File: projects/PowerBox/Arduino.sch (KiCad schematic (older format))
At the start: 59 parts, among them CON3 USB-MINI-B-Vert, IC2 OPAMP-DUALU, P10 CONN_4, P11 CONN_10, P12 CONN_8, P13 CONN_8, P14 CONN_6, P15 CONN_4, P7 CONN_3X2, P8 CONN_4, P9 CONN_4, Q1 MOSFET-P, U3 INA219, U4 AP7333, U5 ATMEGA32U4, X1 16MHz

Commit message: small modifications
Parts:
- added Q?: MOSFET-P, symbol MOSFET-P
- added VR? (x2): VR, symbol VR
- C?: renamed from C5; value 4u7F -> 10uF
- R?: renamed from R21; value 33R -> 22R
- R?: renamed from R22; value 33R -> 22R
- renumbered C3 to C?, C7 to C?, C6 to C?, C12 to C?, C14 to C?, C2 to C?, C1 to C?, C4 to C?, C8 to C?, C9 to C?, C10 to C?, C11 to C?, C13 to C?, CON3 to CON?, D3 to D?, D4 to D?, D5 to D?, D6 to D?, D7 to D?, F1 to F?, IC2 to IC?, JP4 to JP?, JP5 to JP?, JP3 to JP?, L1 to L?, N1 to N?, N2 to N?, N3 to N?, N4 to N?, P11 to P?, P12 to P?, P13 to P?, P14 to P?, P7 to P?, P9 to P?, P10 to P?, P15 to P?, P8 to P?, Q1 to Q?, R24 to R?, R23 to R?, R30 to R?, R28 to R?, R27 to R?, R26 to R?, R29 to R?, R31 to R?, R19 to R?, R20 to R?, R25 to R?, S4 to S?, S5 to S?, U5 to U?, U4 to U?, U3 to U?, X1 to X?
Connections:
- net 3V3: now also IC?.5 (+IN)
- net VREG_in: now also Q?.2 (S); no longer IC?.3 (+IN)
- net XTAL2: now reaches C?.1, R?.2, U?.16 (XTAL2), X?.1
- net XTAL1: now reaches C?.1, R?.1, U?.17 (XTAL1), X?.2
- net at U?.3 (D-): now also R?.2; no longer R?.1
- net at CON?.2 (D-): now also VR?.1; no longer R?.2
- net at R?.2: now also VR?.2; no longer CON?.3 (D+)
- net VCC: now reaches IC?.6 (-IN)
- net VCC: now also IC?.3 (+IN), Q?.3 (D)
- net at IC?.7 (OUT): now also Q?.1 (G)
- new net: R?.1, VR?.2
- new net: CON?.3 (D+), VR?.1
- no-connect marks 10 -> 7
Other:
- note added: "transistor is conducting, when Vgs < 0"
- moved on the sheet: C?, IC?B, JP?, P?, R?, X?

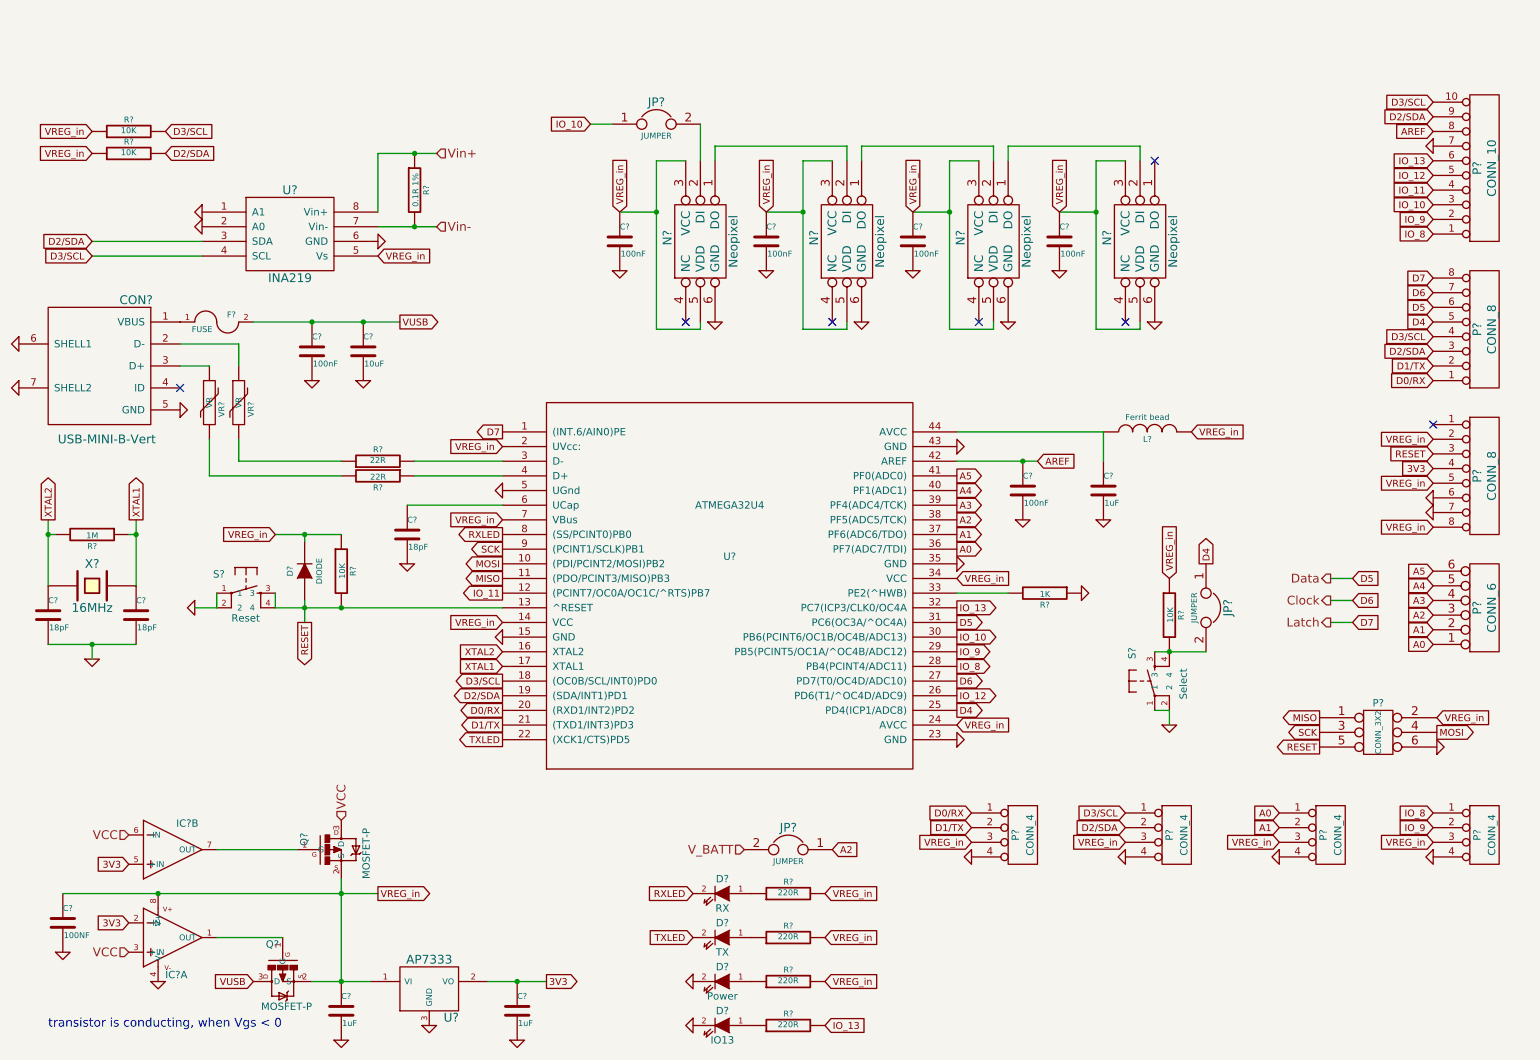
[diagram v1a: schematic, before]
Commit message: erc warnings solved
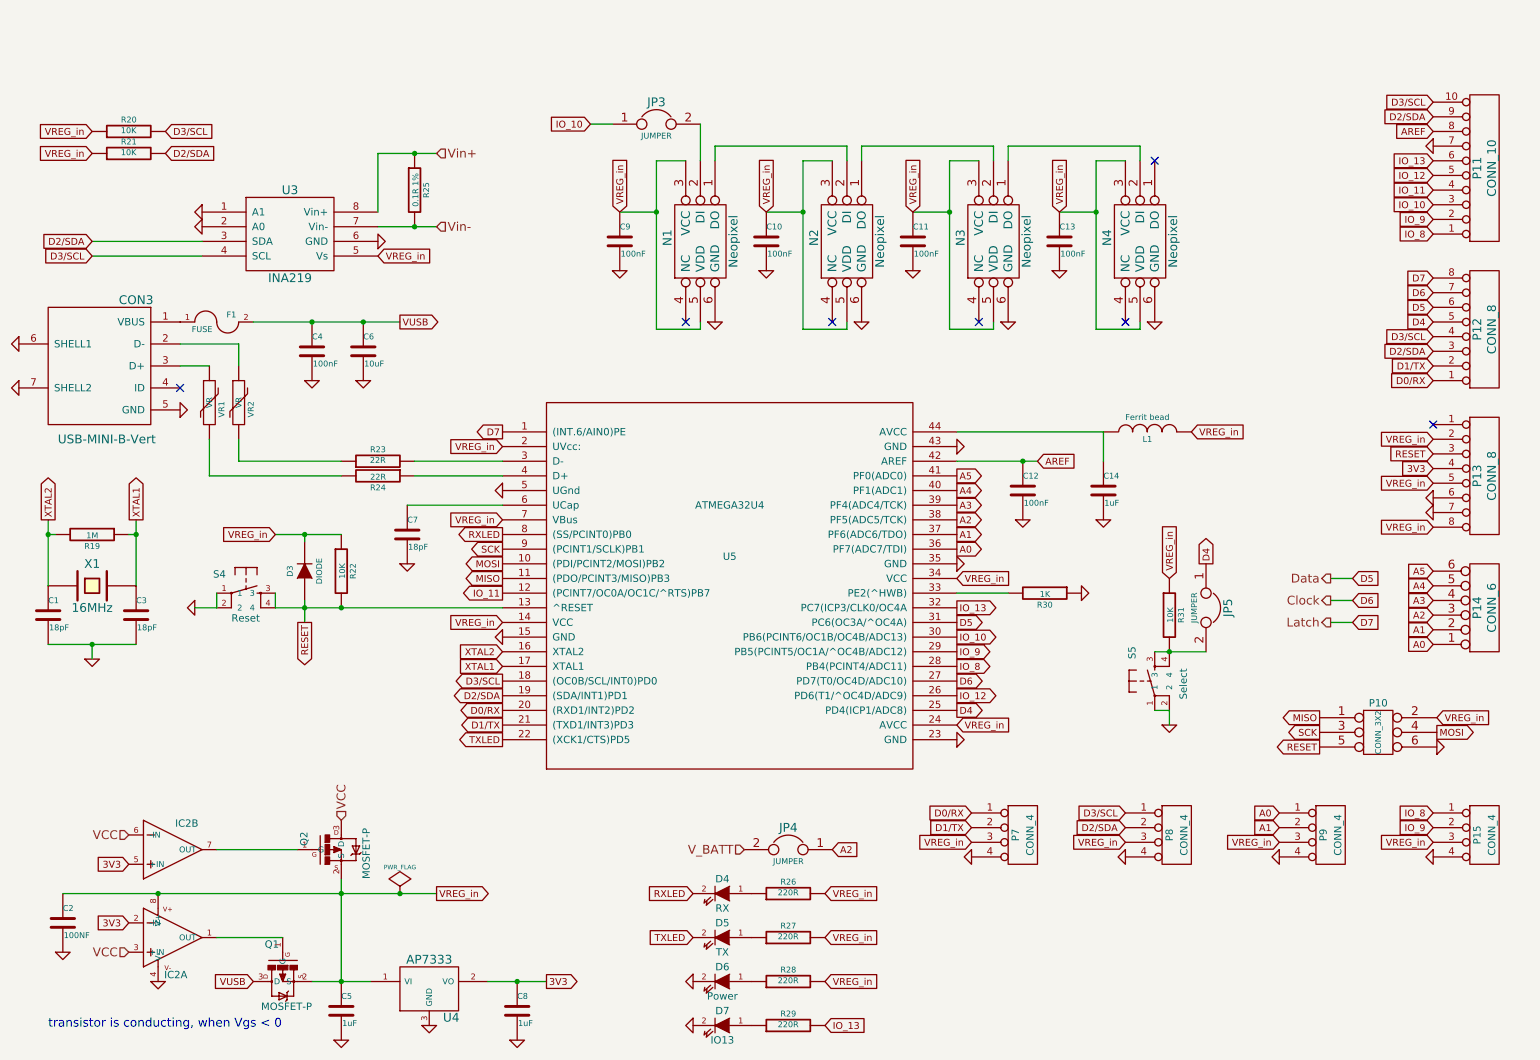
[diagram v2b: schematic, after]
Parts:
- gave numbers to parts that had none: 62

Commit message: more footprints added
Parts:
- C1, C10, C11, C12, C13, C14, C2, C3, C4, C5, C6, C7, C8, C9: footprint (none) -> frep:C0805
- CON3: footprint (none) -> frep:Vertical_USB_Mini_B
- D3, D4, D5, D6, D7: footprint (none) -> frep:LED-0805
- F1, R25: footprint (none) -> frep:R1206
- IC2: footprint SparkFun-SO08 -> frep:SOIC8
- JP3, JP4, JP5: footprint (none) -> frep:Pin_Proto_Straight_1x02
- L1, R19, R20, R21, R22, R23, R24, R26, R27, R28, R29, R30, R31, VR1, VR2: footprint (none) -> frep:R0805
- N1, N2, N3, N4: footprint (none) -> frep:Neopixel
- P10: footprint (none) -> frep:Pin_Proto_Straight_2x03
- P11: footprint (none) -> frep:Pin_Header_Straight_1x10
- P12, P13: footprint (none) -> frep:Pin_Header_Angled_1x08
- P14: footprint (none) -> frep:Pin_Header_Straight_1x06
- P15, P7, P8, P9: footprint (none) -> frep:grove_con_straight
- Q1, Q2, U4: footprint (none) -> frep:SOT23
- S4, S5: footprint TACTILE -> frep:TACTILE-PTH
- U3: footprint (none) -> frep:SOIC8
- U5: footprint MODULE -> frep:TQFP44
- X1: footprint (none) -> frep:HC49UP

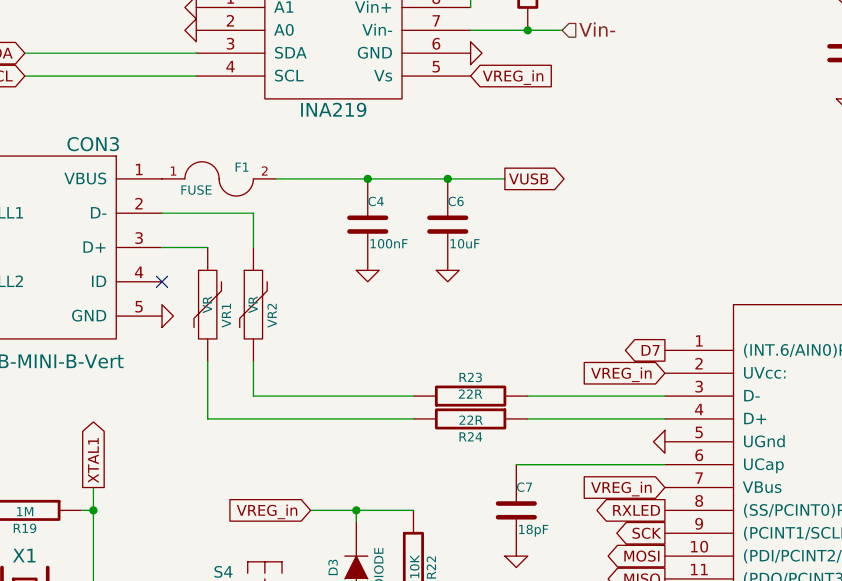
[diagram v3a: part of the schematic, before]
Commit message: protection parts added
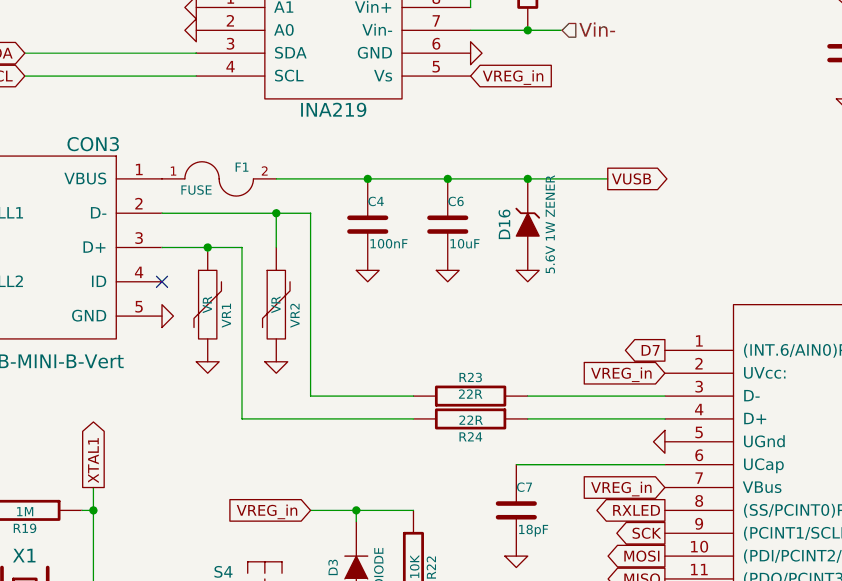
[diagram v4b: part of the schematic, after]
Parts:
- added D16: 5.6V 1W ZENER, symbol ZENER
- F1: footprint frep:R1206 -> frep:C1812
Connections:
- net GND: now also VR1.2, VR2.2, D16.1 (A)
- net VUSB: now also D16.2 (K)
- net at R23.1: now also CON3.2 (D-), VR2.1; no longer VR2.2
- net at R24.2: now also CON3.3 (D+), VR1.1; no longer VR1.2
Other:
- moved on the sheet: VR2

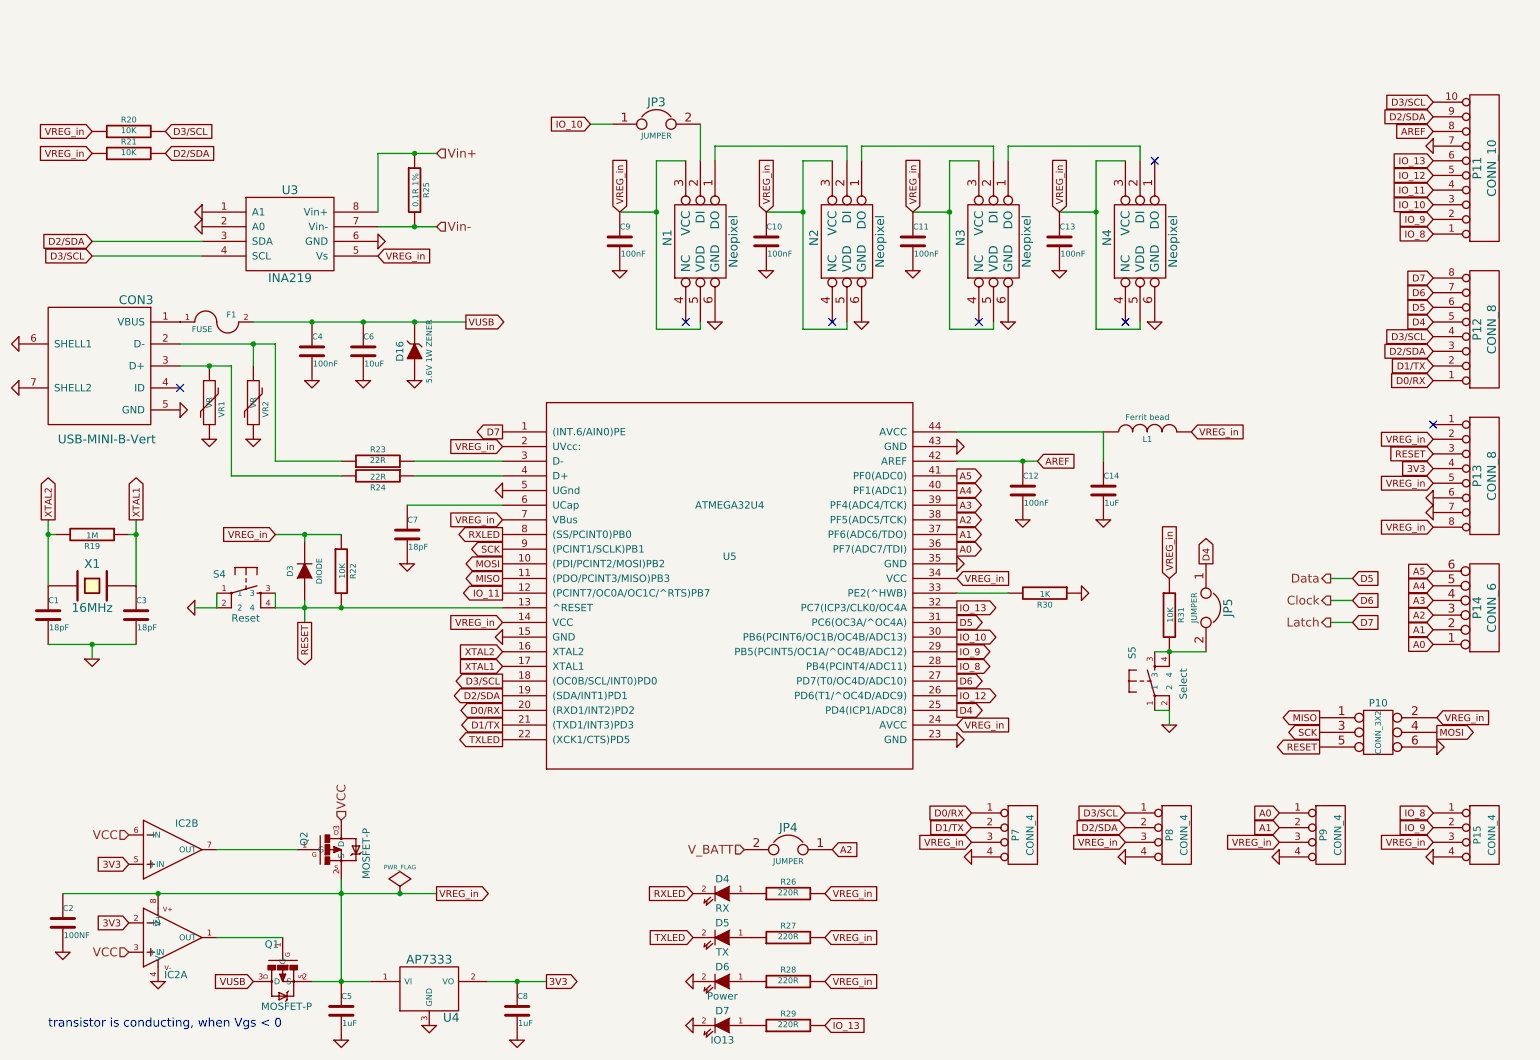
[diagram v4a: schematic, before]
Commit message: Switches changed
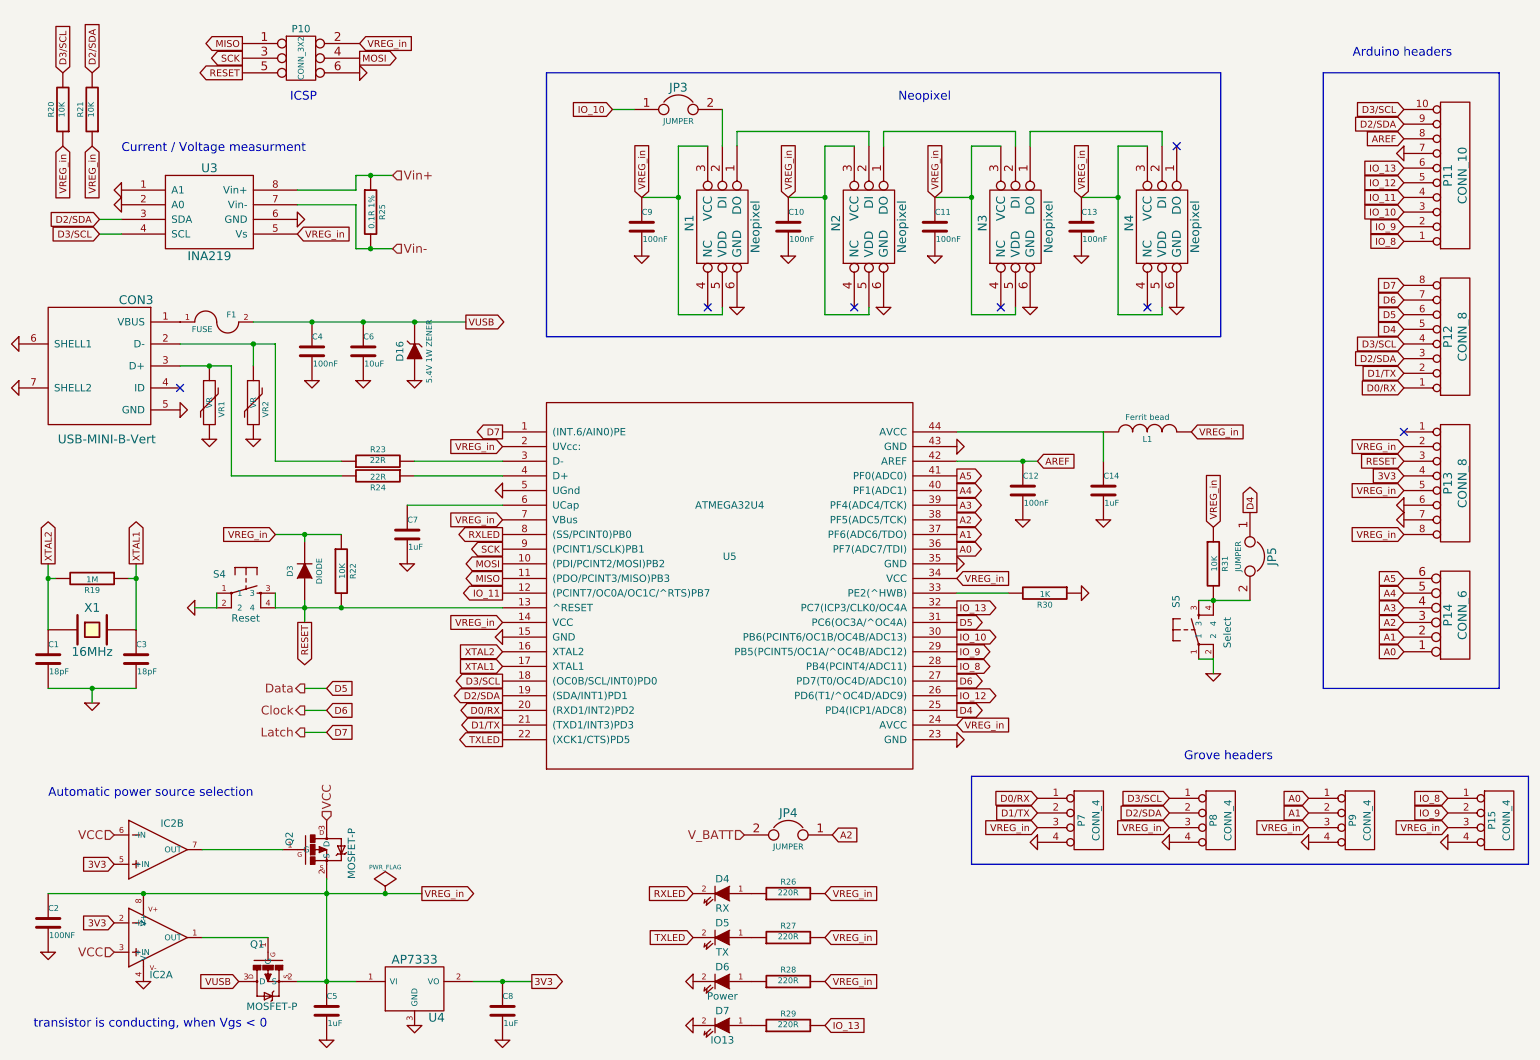
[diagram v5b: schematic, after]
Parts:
- C7: value 18pF -> 1uF
- D16: value 5.6V 1W ZENER -> 5.4V 1W ZENER
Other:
- note added: "Arduino headers"
- note added: "Automatic power source selection"
- note added: "Current / Voltage measurment"
- note added: "Grove headers"
- note added: "ICSP"
- note added: "Neopixel"
- moved on the sheet: C1, C10, C11, C13, C2, C3, C5, C8, C9, IC2A, IC2B, JP3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

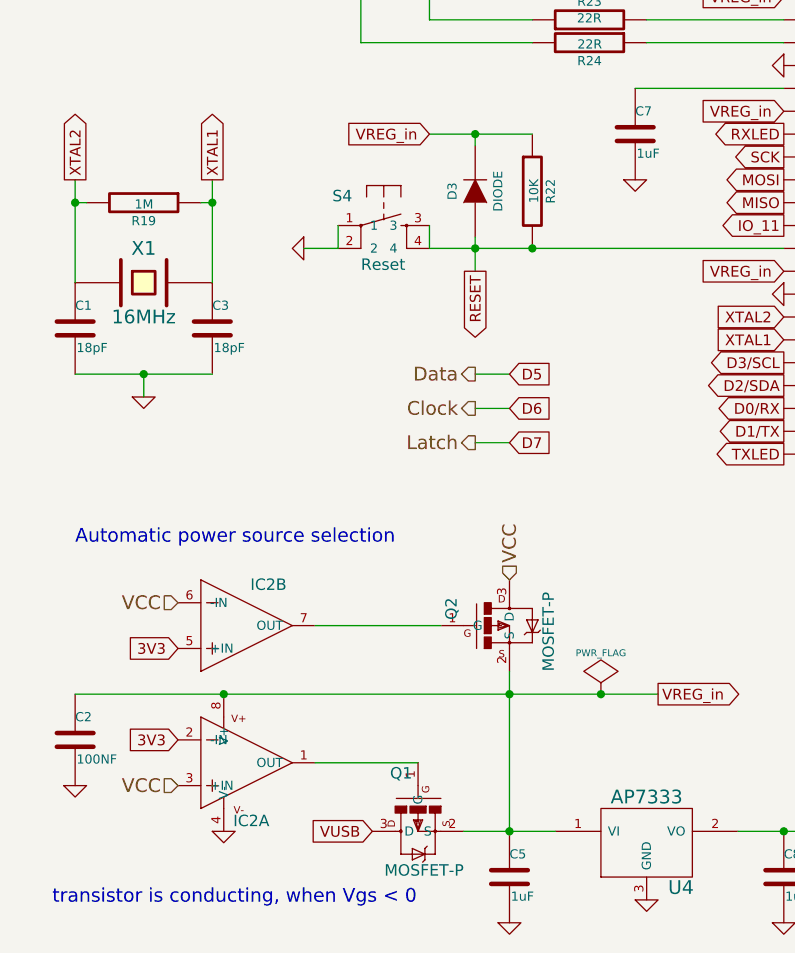
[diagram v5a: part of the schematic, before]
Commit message: part informations added
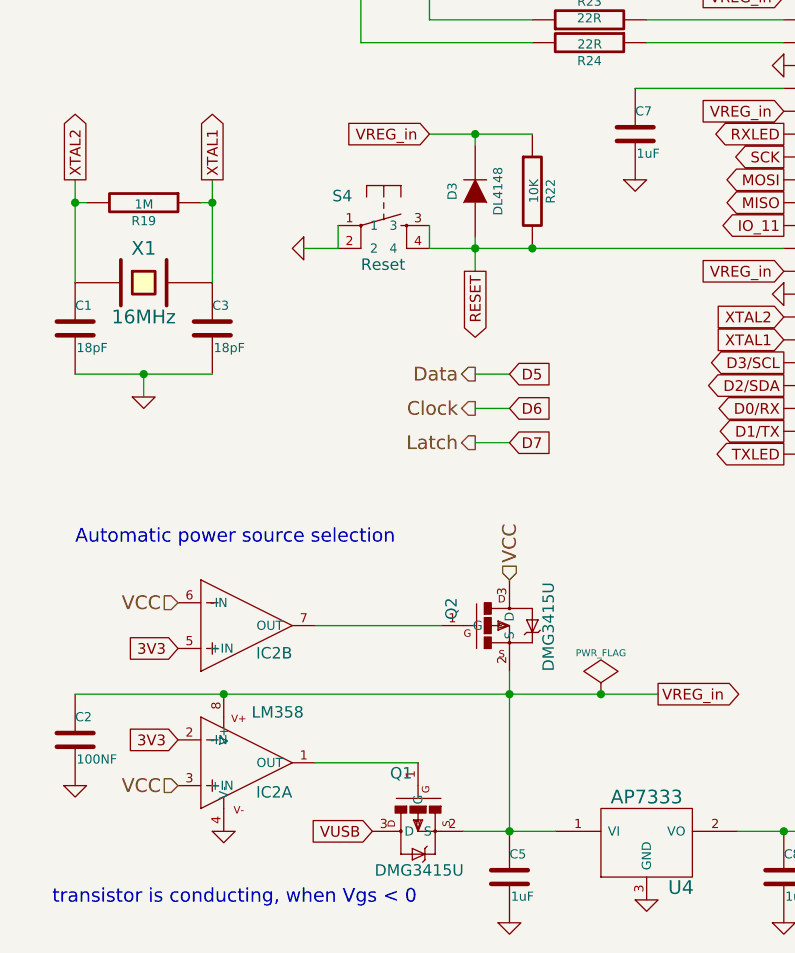
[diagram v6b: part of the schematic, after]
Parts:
- D3: value DIODE -> DL4148
- IC2: value OPAMP-DUALU -> LM358
- Q1, Q2: value MOSFET-P -> DMG3415U

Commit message: netlist finished
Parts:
- removed D16: 5.4V 1W ZENER, symbol ZENER
- added D12: 5.3V Zener, frep:SOT23, symbol ZENER_SOT23
- renumbered C6 to C10, C7 to C11, C8 to C12, C9 to C13, C10 to C14, C11 to C15, C12 to C16, C13 to C17, C14 to C18, C1 to C5, C2 to C6, C3 to C7, C4 to C8, C5 to C9, D3 to D11, D4 to D13, D5 to D14, D6 to D15, D7 to D16, IC2 to IC3, P9 to P10, P10 to P7, P7 to P8, P8 to P9, Q1 to Q4, Q2 to Q5, R20 to R24, R21 to R25, R19 to R26, R22 to R27, R25 to R28, R23 to R29, R24 to R30, R26 to R31, R27 to R32, R28 to R33, R29 to R34, R30 to R35, R31 to R36, U3 to U4, U4 to U5, U5 to U6
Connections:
- net GND: now also D12.1 (A)
- net VUSB: now also D12.3 (K)
- no-connect marks 7 -> 8

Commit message: pcb layout started
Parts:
- D11: footprint frep:LED-0805 -> frep:Diode-MiniMELF_Handsoldering
- P12, P13: footprint frep:Pin_Header_Angled_1x08 -> frep:Pin_Header_Straight_1x08
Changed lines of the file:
@@
 F 0 "P12" V 10450 2800 60  0000 C CNN
 F 1 "CONN_8" V 10550 2800 60  0000 C CNN
-F 2 "frep:Pin_Header_Angled_1x08" H 10500 2800 60  0001 C CNN
+F 2 "frep:Pin_Header_Straight_1x08" H 10500 2800 60  0001 C CNN
 F 3 "" H 10500 2800 60  0000 C CNN
 	1    10500 2800
@@
 F 0 "P13" V 10450 3800 60  0000 C CNN
 F 1 "CONN_8" V 10550 3800 60  0000 C CNN
-F 2 "frep:Pin_Header_Angled_1x08" H 10500 3800 60  0001 C CNN
+F 2 "frep:Pin_Header_Straight_1x08" H 10500 3800 60  0001 C CNN
 F 3 "" H 10500 3800 60  0000 C CNN
 	1    10500 3800
@@
 F 0 "D11" H 2650 4500 40  0000 C CNN
 F 1 "DL4148" H 2650 4300 40  0000 C CNN
-F 2 "frep:LED-0805" H 2650 4400 60  0001 C CNN
+F 2 "frep:Diode-MiniMELF_Handsoldering" H 2650 4400 60  0001 C CNN
 F 3 "" H 2650 4400 60  0000 C CNN
 	1    2650 4400
